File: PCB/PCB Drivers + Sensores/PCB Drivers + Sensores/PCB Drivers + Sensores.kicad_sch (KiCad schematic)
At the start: 38 parts, among them J1 Power, J10 Conn_01x04, J11 Conn_01x04, J12 Conn_01x04, J13 Conn_01x04, J14 Screw_Terminal_01x02, J16 Screw_Terminal_01x02, J17 Conn_01x02, J2 PWM, J3 Analog, J4 PWM, J5 Analog, J6 Communication, J7 Digital, J8 Conn_01x04, J9 Conn_01x04

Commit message: Multplex + Sensores
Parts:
- added Sensor_1, Sensor_10, Sensor_11, Sensor_12, Sensor_2, Sensor_3, Sensor_4, Sensor_5, Sensor_6, Sensor_7, Sensor_8, Sensor_9: Conn_01x07, Connector_PinSocket_2.54mm:PinSocket_1x07_P2.54mm_Vertical, symbol Connector_Generic:Conn_01x07
- added U1: BOB-09056, BOB-09056:MODULE_BOB-09056, symbol BOB-09056:BOB-09056
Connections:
- net *2: now also U1.JP3-7 (S3)
- net *3: now also U1.JP3-6 (S2)
- net *4: now also U1.JP3-5 (S1)
- net *5: now also U1.JP3-4 (S0)
- net +5V: now also Sensor_1.7 (Pin_7), Sensor_10.7 (Pin_7), Sensor_11.7 (Pin_7), Sensor_12.7 (Pin_7), Sensor_2.7 (Pin_7), Sensor_3.7 (Pin_7), Sensor_4.7 (Pin_7), Sensor_5.7 (Pin_7), Sensor_6.7 (Pin_7), Sensor_7.7 (Pin_7), Sensor_8.7 (Pin_7), Sensor_9.7 (Pin_7), U1.JP3-2 (VCC)
- net GND: now also Sensor_1.6 (Pin_6), Sensor_10.6 (Pin_6), Sensor_11.6 (Pin_6), Sensor_12.6 (Pin_6), Sensor_2.6 (Pin_6), Sensor_3.6 (Pin_6), Sensor_4.6 (Pin_6), Sensor_5.6 (Pin_6), Sensor_6.6 (Pin_6), Sensor_7.6 (Pin_6), Sensor_8.6 (Pin_6), Sensor_9.6 (Pin_6), U1.JP3-1 (GND), U1.JP3-3 (EN)
- net *10 renamed LED_4
- net LED_4: now also Sensor_4.1 (Pin_1)
- net *11 renamed LED_3
- net LED_3: now also Sensor_3.1 (Pin_1)
- net *12 renamed LED_2
- net LED_2: now also Sensor_2.1 (Pin_1)
- net *13 renamed LED_1
- net LED_1: now also Sensor_1.1 (Pin_1)
- net *8 renamed LED_6
- net LED_6: now also Sensor_6.1 (Pin_1)
- net *9 renamed LED_5
- net LED_5: now also Sensor_5.1 (Pin_1)
- net RX1/19 renamed LED_12
- net LED_12: now also Sensor_12.1 (Pin_1)
- net RX2/17 renamed LED_10
- net LED_10: now also Sensor_10.1 (Pin_1)
- net RX3/15 renamed LED_8
- net LED_8: now also Sensor_8.1 (Pin_1)
- net SCL/21 renamed SCL
- net SCL: now also Sensor_1.4 (Pin_4), Sensor_10.4 (Pin_4), Sensor_11.4 (Pin_4), Sensor_12.4 (Pin_4), Sensor_2.4 (Pin_4), Sensor_3.4 (Pin_4), Sensor_4.4 (Pin_4), Sensor_5.4 (Pin_4), Sensor_6.4 (Pin_4), Sensor_7.4 (Pin_4), Sensor_8.4 (Pin_4), Sensor_9.4 (Pin_4), U1.JP3-8 (COM)
- net TX1/18 renamed LED_11
- net LED_11: now also Sensor_11.1 (Pin_1)
- net TX2/16 renamed LED_9
- net LED_9: now also Sensor_9.1 (Pin_1)
- net TX3/14 renamed LED_7
- net LED_7: now also Sensor_7.1 (Pin_1)
- new net 3V3: Sensor_1.5 (Pin_5), Sensor_10.5 (Pin_5), Sensor_11.5 (Pin_5), Sensor_12.5 (Pin_5), Sensor_2.5 (Pin_5), Sensor_3.5 (Pin_5), Sensor_4.5 (Pin_5), Sensor_5.5 (Pin_5), Sensor_6.5 (Pin_5), Sensor_7.5 (Pin_5), Sensor_8.5 (Pin_5), Sensor_9.5 (Pin_5)
- new net INT_1: Sensor_1.2 (Pin_2)
- new net INT_10: Sensor_10.2 (Pin_2)
- new net INT_11: Sensor_11.2 (Pin_2)
- new net INT_12: Sensor_12.2 (Pin_2)
- new net INT_2: Sensor_2.2 (Pin_2)
- new net INT_3: Sensor_3.2 (Pin_2)
- new net INT_4: Sensor_4.2 (Pin_2)
- new net INT_5: Sensor_5.2 (Pin_2)
- new net INT_6: Sensor_6.2 (Pin_2)
- new net INT_7: Sensor_7.2 (Pin_2)
- new net INT_8: Sensor_8.2 (Pin_2)
- new net INT_9: Sensor_9.2 (Pin_2)
- new net SDA_1: Sensor_1.3 (Pin_3), U1.JP1-1 (C0)
- new net SDA_10: Sensor_10.3 (Pin_3), U1.JP1-10 (C9)
- new net SDA_11: Sensor_11.3 (Pin_3), U1.JP1-11 (C10)
- new net SDA_12: Sensor_12.3 (Pin_3), U1.JP1-12 (C11)
- new net SDA_2: Sensor_2.3 (Pin_3), U1.JP1-2 (C1)
- new net SDA_3: Sensor_3.3 (Pin_3), U1.JP1-3 (C2)
- new net SDA_4: Sensor_4.3 (Pin_3), U1.JP1-4 (C3)
- new net SDA_5: Sensor_5.3 (Pin_3), U1.JP1-5 (C4)
- new net SDA_6: Sensor_6.3 (Pin_3), U1.JP1-6 (C5)
- new net SDA_7: Sensor_7.3 (Pin_3), U1.JP1-7 (C6)
- new net SDA_8: Sensor_8.3 (Pin_3), U1.JP1-8 (C7)
- new net SDA_9: Sensor_9.3 (Pin_3), U1.JP1-9 (C8)
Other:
- note added: "GPIOs aleatórias"
- moved on the sheet: A1, A2, A3, A4, A5, A6, D1, D2, D3, D4, D5, D6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

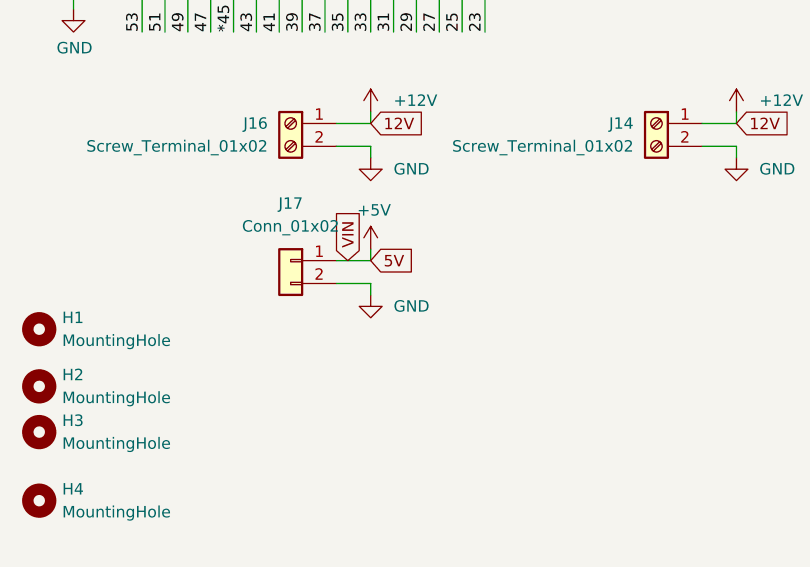
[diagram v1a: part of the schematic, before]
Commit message: Versáo Teste - Trilhas Menores
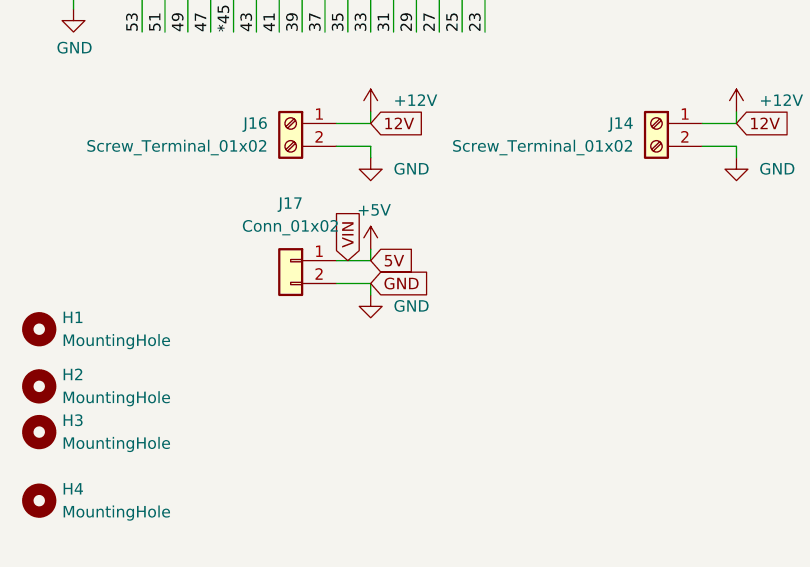
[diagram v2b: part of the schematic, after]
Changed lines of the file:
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@@
+		)
+	)
+	(global_label "GND"
+		(shape input)
+		(at 54.61 170.18 0)
+		(fields_autoplaced yes)
+		(effects
+			(font
+				(size 1.27 1.27)
+			)
+			(justify left)
+		)
+		(property "Intersheetrefs" "${INTERSHEET_REFS}"
+			(at 61.5608 170.18 0)
+			(effects
+				(font
+					(size 1.27 1.27)
+				)
+				(justify left)
+				(hide yes)
+			)
 		)
 	)

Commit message: Versão Final - V1
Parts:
- removed J17: Conn_01x02, Connector_PinSocket_2.54mm:PinSocket_1x02_P2.54mm_Vertical, symbol Connector_Generic:Conn_01x02
- removed Sensor_1, Sensor_10, Sensor_11, Sensor_12, Sensor_2, Sensor_3, Sensor_4, Sensor_5, Sensor_6, Sensor_7, Sensor_8, Sensor_9: Conn_01x07, Connector_PinSocket_2.54mm:PinSocket_1x07_P2.54mm_Vertical, symbol Connector_Generic:Conn_01x07
- added C1, C2, C3, C4, C5, C6: 100uF, Capacitor_THT:CP_Radial_D8.0mm_P3.50mm, symbol Device:C
- added Sensor_1, Sensor_10, Sensor_11, Sensor_12, Sensor_2, Sensor_3, Sensor_4, Sensor_5, Sensor_6, Sensor_7, Sensor_8, Sensor_9: Conn_01x05, Connector_JST:JST_XH_B5B-XH-A_1x05_P2.50mm_Vertical, symbol Connector_Generic:Conn_01x05
- Driver_Conn_1: renamed from J10; footprint Connector_PinSocket_2.54mm:PinSocket_1x04_P2.54mm_Vertical -> Connector_JST:JST_XH_B4B-XH-A_1x04_P2.50mm_Vertical
- Driver_Conn_2: renamed from J8; footprint Connector_PinSocket_2.54mm:PinSocket_1x04_P2.54mm_Vertical -> Connector_JST:JST_XH_B4B-XH-A_1x04_P2.50mm_Vertical
- Driver_Conn_3: renamed from J9; footprint Connector_PinSocket_2.54mm:PinSocket_1x04_P2.54mm_Vertical -> Connector_JST:JST_XH_B4B-XH-A_1x04_P2.50mm_Vertical
- Driver_Conn_4: renamed from J11; footprint Connector_PinSocket_2.54mm:PinSocket_1x04_P2.54mm_Vertical -> Connector_JST:JST_XH_B4B-XH-A_1x04_P2.50mm_Vertical
- Driver_Conn_5: renamed from J12; footprint Connector_PinSocket_2.54mm:PinSocket_1x04_P2.54mm_Vertical -> Connector_JST:JST_XH_B4B-XH-A_1x04_P2.50mm_Vertical
- Driver_Conn_6: renamed from J13; footprint Connector_PinSocket_2.54mm:PinSocket_1x04_P2.54mm_Vertical -> Connector_JST:JST_XH_B4B-XH-A_1x04_P2.50mm_Vertical
- H1, H2, H3, H4: footprint MountingHole:MountingHole_2mm -> MountingHole:MountingHole_6mm
- J1, J3, J4, J5, J6: footprint Connector_PinHeader_2.54mm:PinHeader_1x08_P2.54mm_Vertical -> Connector_PinSocket_2.54mm:PinSocket_1x08_P2.54mm_Vertical
- J7: footprint Connector_PinHeader_2.54mm:PinHeader_2x18_P2.54mm_Vertical -> Connector_PinSocket_2.54mm:PinSocket_2x18_P2.54mm_Vertical
- renumbered J16 to Conn_+12V_1, J14 to JConn_+12V_2
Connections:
- net +12V: now also C1.1, C2.1, C3.1, C4.1, C5.1, C6.1
- net +5V: now also Sensor_1.1 (Pin_1), Sensor_10.1 (Pin_1), Sensor_11.1 (Pin_1), Sensor_12.1 (Pin_1), Sensor_2.1 (Pin_1), Sensor_3.1 (Pin_1), Sensor_4.1 (Pin_1), Sensor_5.1 (Pin_1), Sensor_6.1 (Pin_1), Sensor_7.1 (Pin_1), Sensor_8.1 (Pin_1), Sensor_9.1 (Pin_1)
- net 25: now also A6.9 (~{ENABLE})
- net 27: now also A6.15 (STEP), D6.2 (A)
- net 29: now also A6.16 (DIR)
- net 39: now also A5.9 (~{ENABLE})
- net 41: now also A5.15 (STEP), D5.2 (A)
- net 43: now also A5.16 (DIR)
- net 49: now also A4.9 (~{ENABLE})
- net 51: now also A4.15 (STEP), D4.2 (A)
- net 53: now also A4.16 (DIR)
- net A0: now also A1.16 (DIR)
- net A1: now also A1.15 (STEP), D1.2 (A)
- net A2: now also A1.9 (~{ENABLE})
- net A3: now also A2.16 (DIR)
- net A4: now also A2.15 (STEP), D2.2 (A)
- net A5: now also A2.9 (~{ENABLE})
- net A6: now also A3.16 (DIR)
- net A7: now also A3.15 (STEP), D3.2 (A)
- net A8: now also A3.9 (~{ENABLE})
- net GND: now also C1.2, C2.2, C3.2, C4.2, C5.2, C6.2, Sensor_1.2 (Pin_2), Sensor_10.2 (Pin_2), Sensor_11.2 (Pin_2), Sensor_12.2 (Pin_2), Sensor_2.2 (Pin_2), Sensor_3.2 (Pin_2), Sensor_4.2 (Pin_2), Sensor_5.2 (Pin_2), Sensor_6.2 (Pin_2), Sensor_7.2 (Pin_2), Sensor_8.2 (Pin_2), Sensor_9.2 (Pin_2)
- net LED_1: now also Sensor_1.5 (Pin_5)
- net LED_10: now also Sensor_10.5 (Pin_5)
- net LED_11: now also Sensor_11.5 (Pin_5)
- net LED_12: now also Sensor_12.5 (Pin_5)
- net LED_2: now also Sensor_2.5 (Pin_5)
- net LED_3: now also Sensor_3.5 (Pin_5)
- net LED_4: now also Sensor_4.5 (Pin_5)
- net LED_5: now also Sensor_5.5 (Pin_5)
- net LED_6: now also Sensor_6.5 (Pin_5)
- net LED_7: now also Sensor_7.5 (Pin_5)
- net LED_8: now also Sensor_8.5 (Pin_5)
- net LED_9: now also Sensor_9.5 (Pin_5)
- net SCL: now also Sensor_1.3 (Pin_3), Sensor_10.3 (Pin_3), Sensor_11.3 (Pin_3), Sensor_12.3 (Pin_3), Sensor_2.3 (Pin_3), Sensor_3.3 (Pin_3), Sensor_4.3 (Pin_3), Sensor_5.3 (Pin_3), Sensor_6.3 (Pin_3), Sensor_7.3 (Pin_3), Sensor_8.3 (Pin_3), Sensor_9.3 (Pin_3)
- net SDA_1: now also Sensor_1.4 (Pin_4)
- net SDA_10: now also Sensor_10.4 (Pin_4)
- net SDA_11: now also Sensor_11.4 (Pin_4)
- net SDA_12: now also Sensor_12.4 (Pin_4)
- net SDA_2: now also Sensor_2.4 (Pin_4)
- net SDA_3: now also Sensor_3.4 (Pin_4)
- net SDA_4: now also Sensor_4.4 (Pin_4)
- net SDA_5: now also Sensor_5.4 (Pin_4)
- net SDA_6: now also Sensor_6.4 (Pin_4)
- net SDA_7: now also Sensor_7.4 (Pin_4)
- net SDA_8: now also Sensor_8.4 (Pin_4)
- net SDA_9: now also Sensor_9.4 (Pin_4)
- net at A5.12 (MS3): no longer D5.2 (A)
- net at A4.12 (MS3): no longer D4.2 (A)
- net at A6.12 (MS3): no longer D6.2 (A)
- net at A1.12 (MS3): no longer D1.2 (A)
- net at A5.13 (~{RESET}): now also A5.14 (~{SLEEP})
- net at A2.12 (MS3): no longer D2.2 (A)
- net at A3.12 (MS3): no longer D3.2 (A)
- net at A4.13 (~{RESET}): now also A4.14 (~{SLEEP})
- net at A3.13 (~{RESET}): now also A3.14 (~{SLEEP})
- net at A6.13 (~{RESET}): now also A6.14 (~{SLEEP})
- net at A1.13 (~{RESET}): now also A1.14 (~{SLEEP})
- net at A2.13 (~{RESET}): now also A2.14 (~{SLEEP})
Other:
- moved on the sheet: D1, D2, D3, D4, D5, D6, R1, R2, R3, R4, R5, R6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

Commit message: Placa Final - +Leds +Botão
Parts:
- added D7, D8: LED, LED_THT:LED_D5.0mm, symbol Device:LED
- added R7: 330, Resistor_THT:R_Axial_DIN0207_L6.3mm_D2.5mm_P10.16mm_Horizontal, symbol Device:R
- added R8: 1k, Resistor_THT:R_Axial_DIN0207_L6.3mm_D2.5mm_P10.16mm_Horizontal, symbol Device:R
- added SW1: SW_Push, Button_Switch_THT:SW_PUSH_6mm, symbol Switch:SW_Push
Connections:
- net +12V: now also R8.1
- net +5V: now also R7.1
- net GND: now also D7.1 (K), D8.1 (K), SW1.2
- net ~{RESET}: now also SW1.1
- new net: D7.2 (A), R7.2
- new net: D8.2 (A), R8.2
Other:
- moved on the sheet: Conn_+12V_1, H1, H2, H3, H4, JConn_+12V_2, Sensor_1, Sensor_10, Sensor_11, Sensor_12, Sensor_2, Sensor_3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

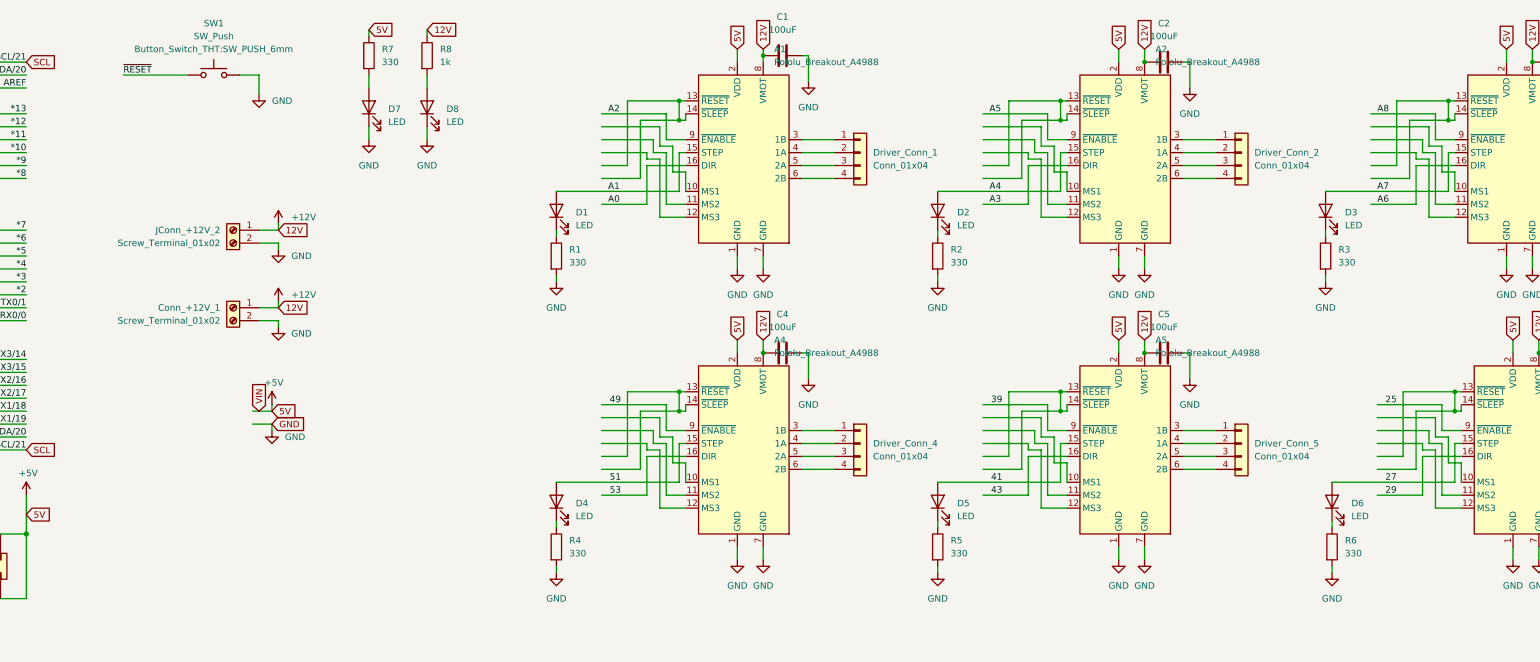
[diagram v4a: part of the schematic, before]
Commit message: +LEDs, +BARREL JACK
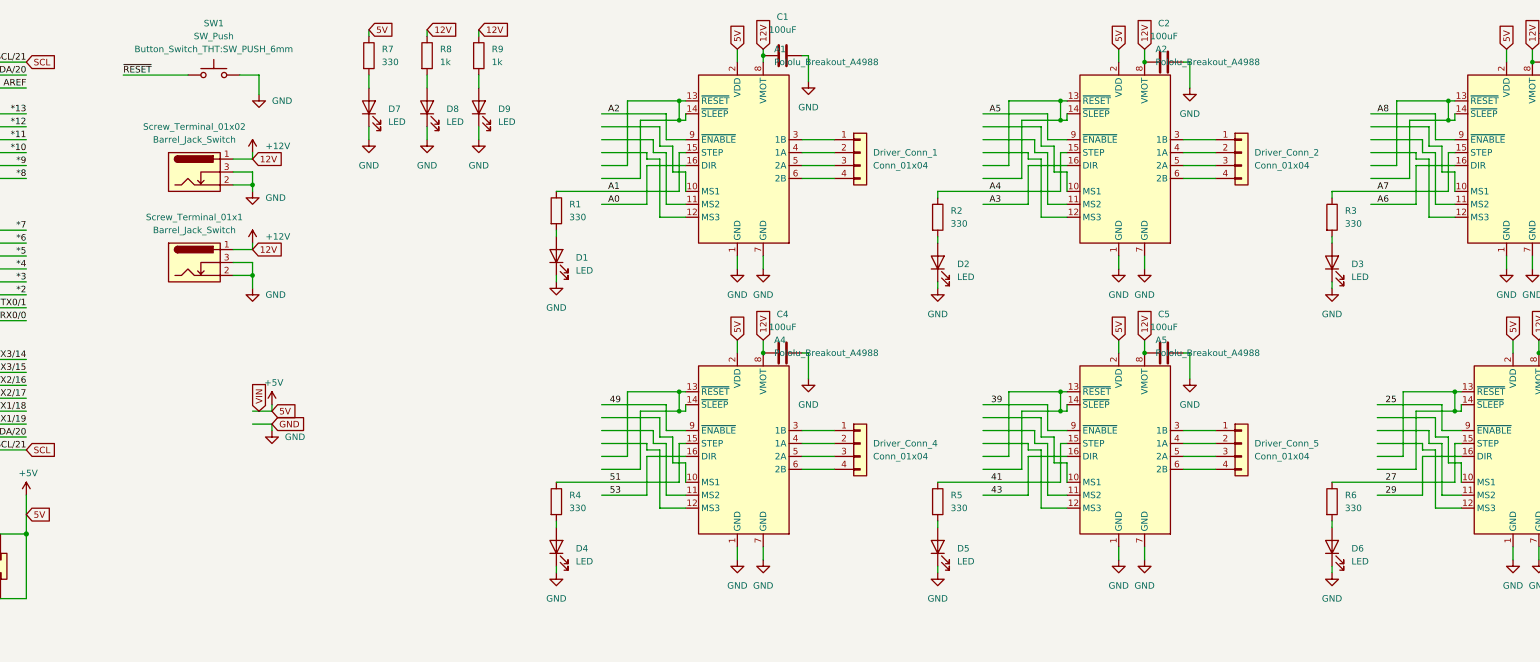
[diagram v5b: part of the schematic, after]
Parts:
- removed Conn_+12V_1, JConn_+12V_2: Screw_Terminal_01x02, TerminalBlock_RND:TerminalBlock_RND_205-00298_1x02_P10.00mm_Horizontal, symbol Connector:Screw_Terminal_01x02
- added D9: LED, LED_THT:LED_D5.0mm, symbol Device:LED
- added R9: 1k, Resistor_THT:R_Axial_DIN0207_L6.3mm_D2.5mm_P10.16mm_Horizontal, symbol Device:R
- added Screw_Terminal_01x02, Screw_Terminal_01x1: Barrel_Jack_Switch, Connector_BarrelJack:BarrelJack_Horizontal, symbol Connector:Barrel_Jack_Switch
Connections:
- net +12V: now also R9.1, Screw_Terminal_01x02.1, Screw_Terminal_01x1.1
- net 27: now also R6.1; no longer D6.2 (A)
- net 41: now also R5.1; no longer D5.2 (A)
- net 51: now also R4.1; no longer D4.2 (A)
- net A1: now also R1.1; no longer D1.2 (A)
- net A4: now also R2.1; no longer D2.2 (A)
- net A7: now also R3.1; no longer D3.2 (A)
- net GND: now also D1.1 (K), D2.1 (K), D3.1 (K), D4.1 (K), D5.1 (K), D6.1 (K), D9.1 (K), Screw_Terminal_01x02.2, Screw_Terminal_01x02.3, Screw_Terminal_01x1.2, Screw_Terminal_01x1.3; no longer R1.2, R2.2, R3.2, R4.2, R5.2, R6.2
- new net: D5.2 (A), R5.2
- new net: D1.2 (A), R1.2
- new net: D4.2 (A), R4.2
- new net: D6.2 (A), R6.2
- new net: D2.2 (A), R2.2
- new net: D3.2 (A), R3.2
- new net: D9.2 (A), R9.2
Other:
- moved on the sheet: D1, D2, D3, D4, D5, D6, R1, R2, R3, R4, R5, R6

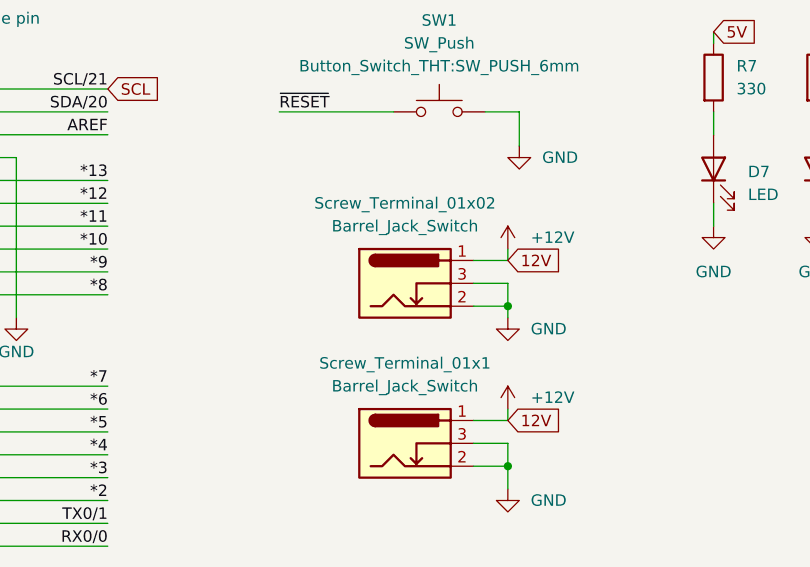
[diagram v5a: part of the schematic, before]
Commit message: Logos no Silkscreen
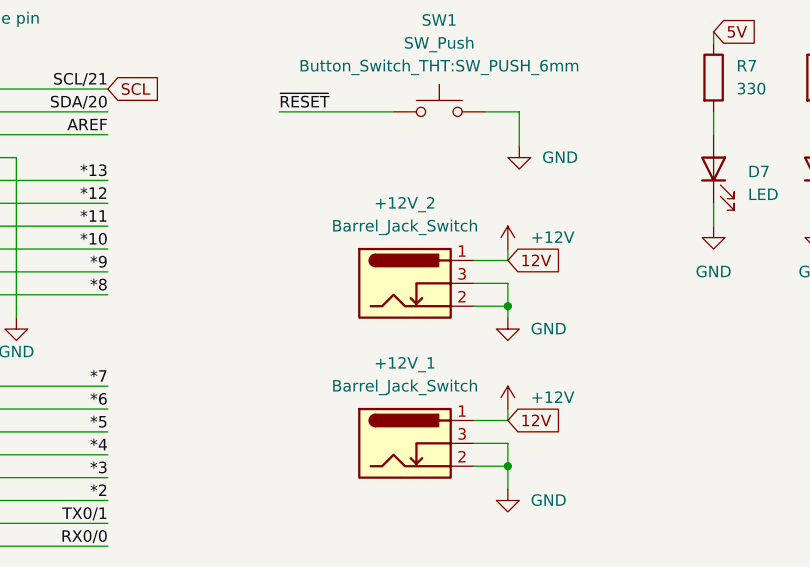
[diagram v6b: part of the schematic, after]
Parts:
- renumbered Screw_Terminal_01x1 to +12V_1, Screw_Terminal_01x02 to +12V_2
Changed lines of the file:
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@@
 		(dnp no)
 		(fields_autoplaced yes)
-		(property "Reference" "Screw_Terminal_01x02"
+		(property "Reference" "+12V_2"
 			(at 107.95 39.37 0)
 			(effects
@@
 			(project ""
 				(path "/e63e39d7-6ac0-4ffd-8aa3-1841a4541b55"
-					(reference "Screw_Terminal_01x02")
+					(reference "+12V_2")
 					(unit 1)
 				)
@@
 		(dnp no)
 		(fields_autoplaced yes)
-		(property "Reference" "Screw_Terminal_01x1"
+		(property "Reference" "+12V_1"
 			(at 107.95 57.15 0)
 			(effects
@@
 			(project "PCB Drivers + Sensores"
 				(path "/e63e39d7-6ac0-4ffd-8aa3-1841a4541b55"
-					(reference "Screw_Terminal_01x1")
+					(reference "+12V_1")
 					(unit 1)
 				)
